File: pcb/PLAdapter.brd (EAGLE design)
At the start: 35.6 x 20.3 mm, 2 parts, among them IC1 PLA, IC2 EPROM

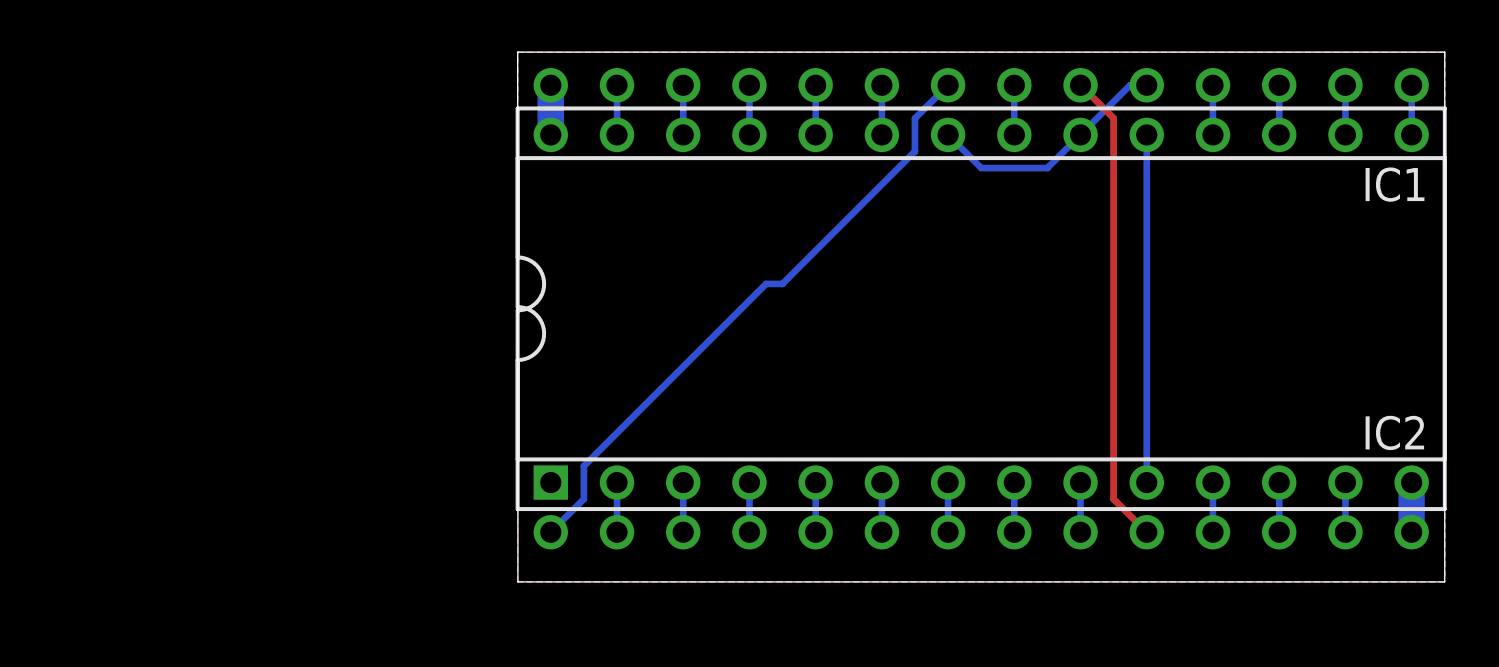
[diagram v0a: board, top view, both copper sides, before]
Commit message: Round edges of PCB and recreate gerbers
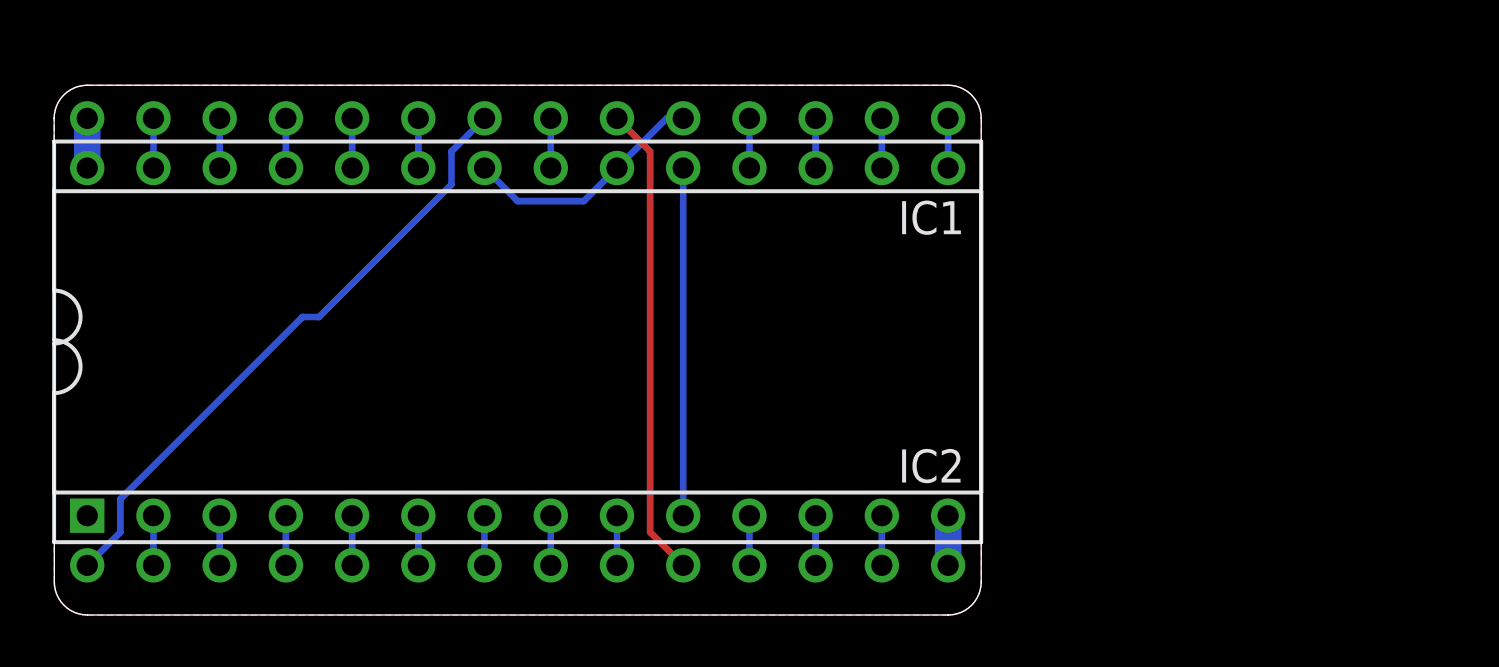
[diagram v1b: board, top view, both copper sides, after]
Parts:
- moved IC1 17.8 mm to (0.00, 11.4)
- moved IC2 17.8 mm to (0.00, 9.53)
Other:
- outline, holes or cut-outs redrawn
